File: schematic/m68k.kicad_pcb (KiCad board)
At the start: 2 copper layers, 176.1 x 104 mm, 45 parts, among them J1 CONN_02X03, J2 CONN_01X03, J3 JTAG, J4 CONN_02X30, J5 I2C, J6 CONN_02X30, J7 CONN_01X02, J8 CONN_02X30, J9 CONN_01X03, SW1 SW_Push_Dual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

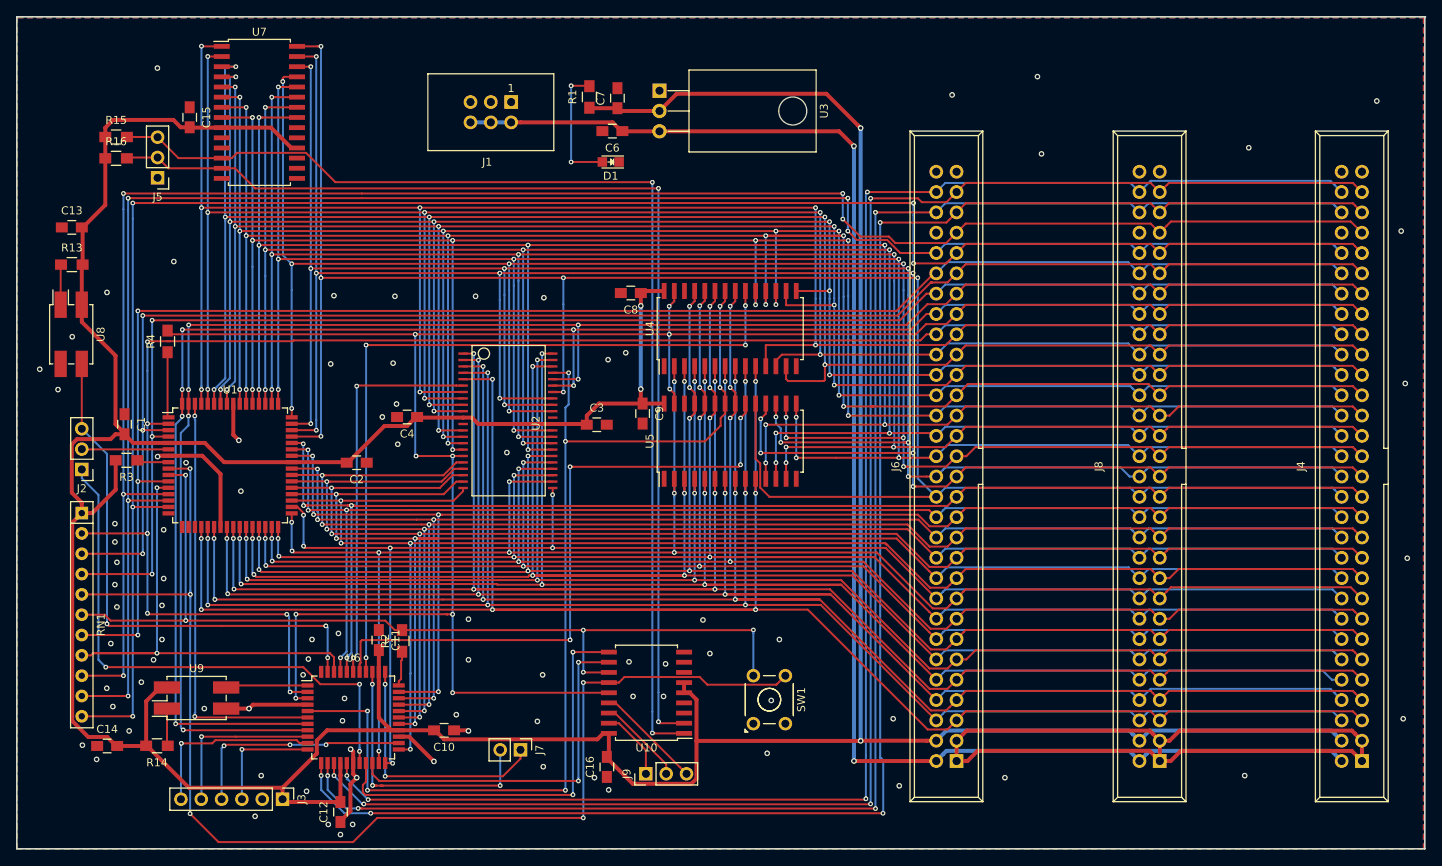
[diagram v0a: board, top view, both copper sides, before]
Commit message: mounting holes missing
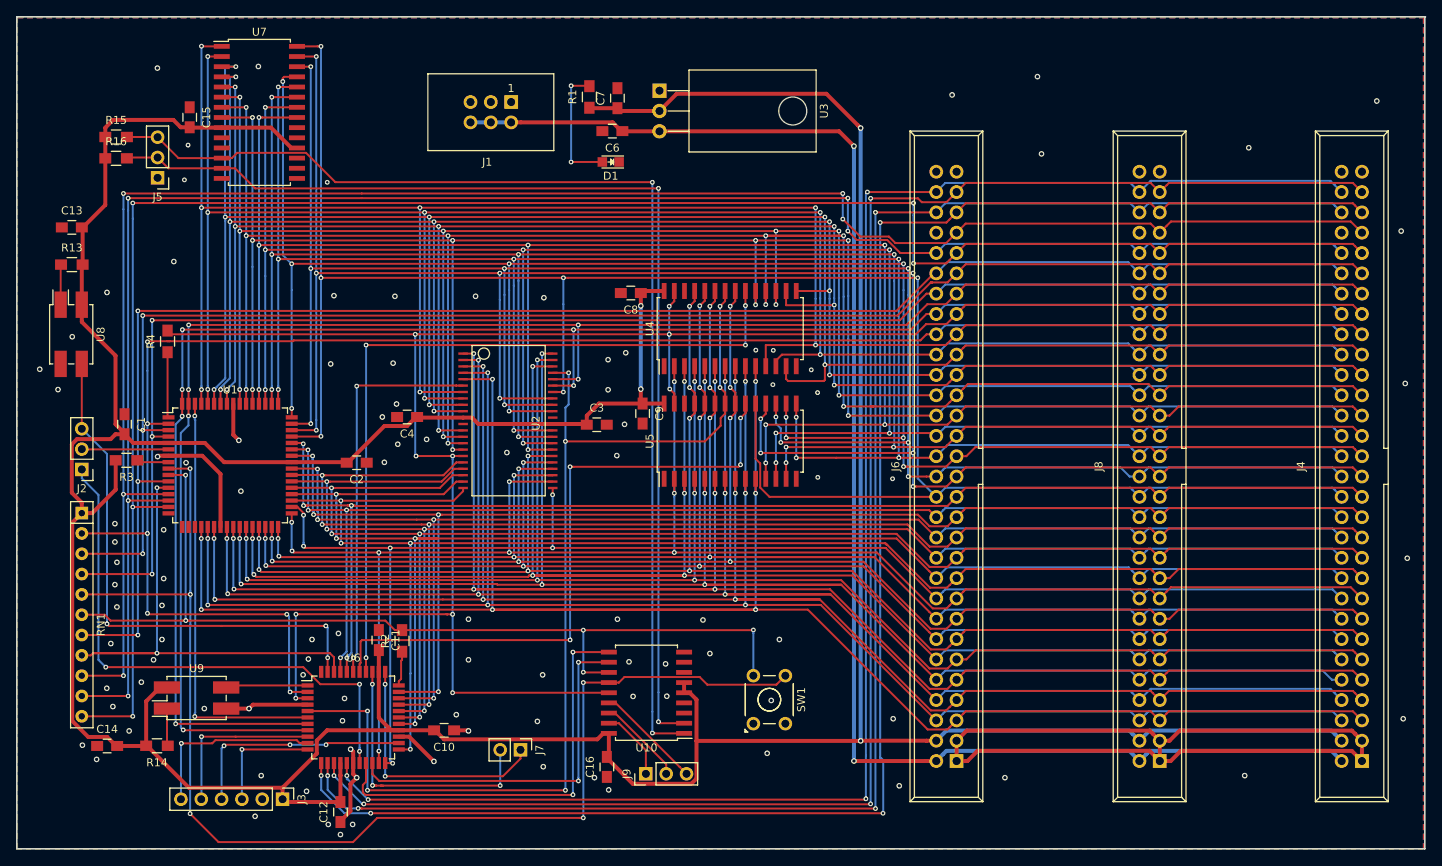
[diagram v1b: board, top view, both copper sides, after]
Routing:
- net (no net): track 0.02 -> 0.00 mm, vias 80 -> 0
- net GND: vias 7 -> 104

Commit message: mounting holes added
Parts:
- added REF**: 1pin, Connectors:1pin, F.Cu at (73.7, 121.9)
- added REF**: 1pin, Connectors:1pin, F.Cu at (223.5, 121.9)
- added REF**: 1pin, Connectors:1pin, F.Cu at (73.7, 27.9)
- added REF**: 1pin, Connectors:1pin, F.Cu at (223.5, 27.9)
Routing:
- net GND: vias 104 -> 7
- net (no net): vias 0 -> 97

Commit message: layout done again
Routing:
- net GND: vias 7 -> 104
- net (no net): vias 97 -> 0

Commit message: done.
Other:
- board text added: "m68k computer rev. 1"
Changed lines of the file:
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@@
-(kicad_pcb (version 4) (host pcbnew 4.0.6)
+(kicad_pcb (version 20170123) (host pcbnew "(2017-09-01 revision 8d14751)-master")
   (general
-    (links 420)
-    (no_connects 8)
-    (area 67.899999 22.899999 244.194001 127.100001)
     (thickness 1.6)
-    (drawings 4)
+    (drawings 5)
     (tracks 2476)
     (zones 0)
@@
     (visible_elements FFFFFF7F)
     (pcbplotparams
-      (layerselection 0x3c0ff_ffffffff)
-      (usegerberextensions false)
+      (layerselection 0x010f0_ffffffff)
+      (usegerberextensions true)
+      (usegerberattributes true)
+      (usegerberadvancedattributes true)
+      (creategerberjobfile true)
       (excludeedgelayer true)
       (linewidth 0.100000)
@@
       (hpglpenspeed 20)
       (hpglpendiameter 15)
-      (hpglpenoverlay 2)
       (psnegative false)
       (psa4output false)
-      (plotreference false)
-      (plotvalue false)
+      (plotreference true)
+      (plotvalue true)
       (plotinvisibletext false)
       (padsonsilk false)
@@
     (descr "module 1 pin (ou trou mecanique de percage)")
     (tags DEV)
-    (fp_text reference REF** (at 0 -3.048) (layer F.SilkS)
+    (fp_text reference REF** (at 0 -3.048) (layer F.SilkS) hide
       (effects (font (size 1 1) (thickness 0.15)))
     )
@@
     (descr "module 1 pin (ou trou mecanique de percage)")
     (tags DEV)
-    (fp_text reference REF** (at 0 -3.048) (layer F.SilkS)
+    (fp_text reference REF** (at 0 -3.048) (layer F.SilkS) hide
       (effects (font (size 1 1) (thickness 0.15)))
     )
@@
     (tags "resistor 0805")
     (attr smd)
-    (fp_text reference R15 (at 0 -2.1) (layer F.SilkS)
-      (effects (font (size 1 1) (thickness 0.15)))
-    )
-    (fp_text value 2k (at 0 2.1) (layer F.Fab)
+    (fp_text reference R15 (at -4.1402 -0.1016) (layer F.SilkS)
+      (effects (font (size 1 1) (thickness 0.15)))
+    )
+    (fp_text value 2k (at -0.0254 -1.778) (layer F.Fab)
       (effects (font (size 1 1) (thickness 0.15)))
     )
@@
     (tags "resistor 0805")
     (attr smd)
-    (fp_text reference R16 (at 0 -2.1) (layer F.SilkS)
+    (fp_text reference R16 (at -4.3142 -0.0508) (layer F.SilkS)
       (effects (font (size 1 1) (thickness 0.15)))
     )
@@
     (tags "capacitor 0805")
     (attr smd)
-    (fp_text reference C1 (at 0 -2.1 270) (layer F.SilkS)
+    (fp_text reference C1 (at -3.623 -0.3222 270) (layer F.SilkS)
       (effects (font (size 1 1) (thickness 0.15)))
     )
@@
     (tags "capacitor 0805")
     (attr smd)
-    (fp_text reference C6 (at 0 -2.1 180) (layer F.SilkS)
+    (fp_text reference C6 (at 3.3274 -0.127 180) (layer F.SilkS)
       (effects (font (size 1 1) (thickness 0.15)))
     )
@@
     (tags "capacitor 0805")
     (attr smd)
-    (fp_text reference C7 (at 0 -2.1 90) (layer F.SilkS)
+    (fp_text reference C7 (at 3.4544 0.127 90) (layer F.SilkS)
       (effects (font (size 1 1) (thickness 0.15)))
     )
@@
     (tags "capacitor 0805")
     (attr smd)
-    (fp_text reference C11 (at 0 -2.1 270) (layer F.SilkS)
+    (fp_text reference C11 (at -3.9316 -0.0508 270) (layer F.SilkS)
       (effects (font (size 1 1) (thickness 0.15)))
     )
@@
     (tags "capacitor 0805")
     (attr smd)
-    (fp_text reference C13 (at 0 -2.1) (layer F.SilkS)
-      (effects (font (size 1 1) (thickness 0.15)))
-    )
-    (fp_text value 100n (at 0 2.1) (layer F.Fab)
+    (fp_text reference C13 (at 0.0254 -1.9558) (layer F.SilkS)
+      (effects (font (size 1 1) (thickness 0.15)))
+    )
+    (fp_text value 100n (at 4.2418 -0.1016) (layer F.Fab)
       (effects (font (size 1 1) (thickness 0.15)))
     )
@@
     (tags "capacitor 0805")
     (attr smd)
-    (fp_text reference C14 (at 0 -2.1) (layer F.SilkS)
+    (fp_text reference C14 (at -4.3634 -0.2286) (layer F.SilkS)
       (effects (font (size 1 1) (thickness 0.15)))
     )
@@
     (tags "capacitor 0805")
     (attr smd)
-    (fp_text reference C15 (at 0 -2.1 270) (layer F.SilkS)
-      (effects (font (size 1 1) (thickness 0.15)))
-    )
-    (fp_text value 100n (at 0 2.1 270) (layer F.Fab)
+    (fp_text reference C15 (at -4.064 0.0762 270) (layer F.SilkS)
+      (effects (font (size 1 1) (thickness 0.15)))
+    )
+    (fp_text value 100n (at -0.1016 -1.778 270) (layer F.Fab)
       (effects (font (size 1 1) (thickness 0.15)))
     )
@@
     (tags "LED 0805 SMD")
     (attr smd)
-    (fp_text reference D1 (at 0 -1.75 180) (layer F.SilkS)
+    (fp_text reference D1 (at 2.921 -0.0254 180) (layer F.SilkS)
       (effects (font (size 1 1) (thickness 0.15)))
     )
@@
     (descr "Through hole straight pin header, 1x03, 2.54mm pitch, single row")
     (tags "Through hole pin header THT 1x03 2.54mm single row")
-    (fp_text reference J9 (at 0 -2.39 90) (layer F.SilkS)
+    (fp_text reference J9 (at -2.6924 0.1016 180) (layer F.SilkS)
       (effects (font (size 1 1) (thickness 0.15)))
     )
@@
     (tags "resistor 0805")
     (attr smd)
-    (fp_text reference R1 (at 0 -2.1 90) (layer F.SilkS)
+    (fp_text reference R1 (at 3.7846 -0.0762 90) (layer F.SilkS)
       (effects (font (size 1 1) (thickness 0.15)))
     )
@@
     (tags "resistor 0805")
     (attr smd)
-    (fp_text reference R3 (at 0 -2.1 180) (layer F.SilkS)
+    (fp_text reference R3 (at 0 -2.0828 180) (layer F.SilkS)
       (effects (font (size 1 1) (thickness 0.15)))
     )
@@
       (effects (font (size 1 1) (thickness 0.15)))
     )
-    (fp_text value 10k (at 0 2.1) (layer F.Fab)
+    (fp_text value 10k (at 4.0132 0) (layer F.Fab)
       (effects (font (size 1 1) (thickness 0.15)))
     )
@@
     (tags "resistor 0805")
     (attr smd)
-    (fp_text reference R14 (at 0 -2.1 180) (layer F.SilkS)
+    (fp_text reference R14 (at -4.2164 0.0254 180) (layer F.SilkS)
       (effects (font (size 1 1) (thickness 0.15)))
     )
@@
     (descr SW_TH_Tactile_Omron_B3F-10xx)
     (tags "Omron B3F-10xx")
-    (fp_text reference SW1 (at 3 6 90) (layer F.SilkS)
+    (fp_text reference SW1 (at -2.3566 1.905) (layer F.SilkS)
       (effects (font (size 1 1) (thickness 0.15)))
     )
@@
     (tags "resistor 0805")
     (attr smd)
-    (fp_text reference R2 (at 0 -2.1 90) (layer F.SilkS)
+    (fp_text reference R2 (at 3.5814 0 90) (layer F.SilkS)
       (effects (font (size 1 1) (thickness 0.15)))
     )
@@
     (descr "module 1 pin (ou trou mecanique de percage)")
     (tags DEV)
-    (fp_text reference REF** (at 0 -3.048) (layer F.SilkS)
+    (fp_text reference REF** (at 0 -3.048) (layer F.SilkS) hide
       (effects (font (size 1 1) (thickness 0.15)))
     )
@@
     (descr "module 1 pin (ou trou mecanique de percage)")
     (tags DEV)
-    (fp_text reference REF** (at 0 -3.048) (layer F.SilkS)
+    (fp_text reference REF** (at 0 -3.048) (layer F.SilkS) hide
       (effects (font (size 1 1) (thickness 0.15)))
     )
@@
     (fp_circle (center 0 0) (end 0 -2.286) (layer F.SilkS) (width 0.12))
     (pad 1 thru_hole circle (at 0 0) (size 4.064 4.064) (drill 3.048) (layers *.Cu *.Mask))
+  )
+  (gr_text "m68k computer rev. 1" (at 191.008 26.3652) (layer F.SilkS)
+    (effects (font (size 1.5 1.5) (thickness 0.3)))
   )
   (gr_line (start 68 127) (end 68 23) (layer Edge.Cuts) (width 0.2))
@@
   (via (at 85.5726 29.4132) (size 0.7) (drill 0.4) (layers F.Cu B.Cu) (net 1))
   (via (at 184.912 32.766) (size 0.7) (drill 0.4) (layers F.Cu B.Cu) (net 1))
-  (via (at 195.58 30.48) (size 0.7) (drill 0.4) (layers F.Cu B.Cu) (net 1))
+  (via (at 205.105 32.6136) (size 0.7) (drill 0.4) (layers F.Cu B.Cu) (net 1))
   (segment (start 86.9658 77.8702) (end 85.7058 77.8702) (width 0.5) (layer F.Cu) (net 1))
   (segment (start 85.7058 77.8702) (end 85.598 77.978) (width 0.5) (layer F.Cu) (net 1))
